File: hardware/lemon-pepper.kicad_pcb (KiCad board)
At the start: 4 copper layers, 35 x 35 mm, 87 parts, among them J101 INPUT, J201 USB_C_Receptacle_USB2.0, J301 TagConnect, J302 USER CONN., M101 MOT, Q501 MMBT5551, SW301 USER, U201 SRV05-4, U301 STM32G431, U302 SN65HVD230, U401 MT6835, U501 MAX15062AATA+T, U601 L6226QTR, U701 MAX49925, U703 MAX49925, Y301 12MHz

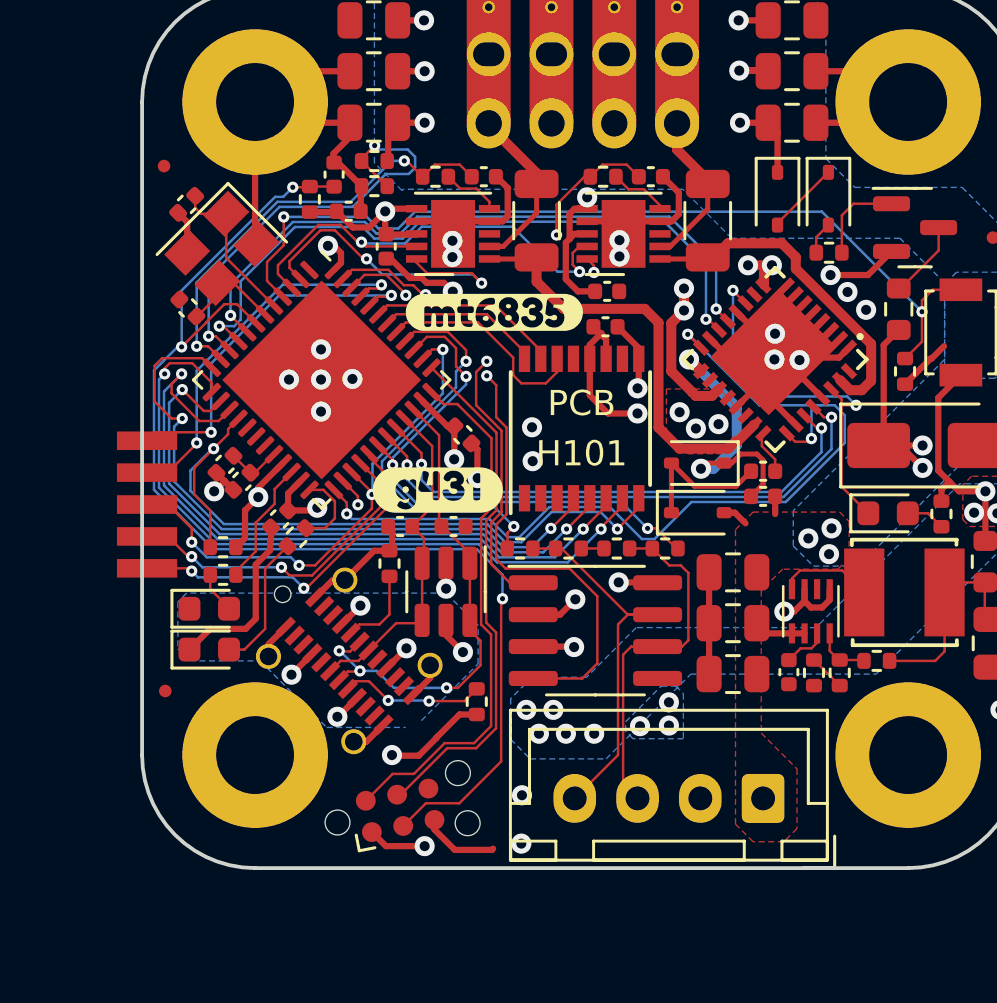
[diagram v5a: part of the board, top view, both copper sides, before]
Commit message: add tooling holes, update CPL
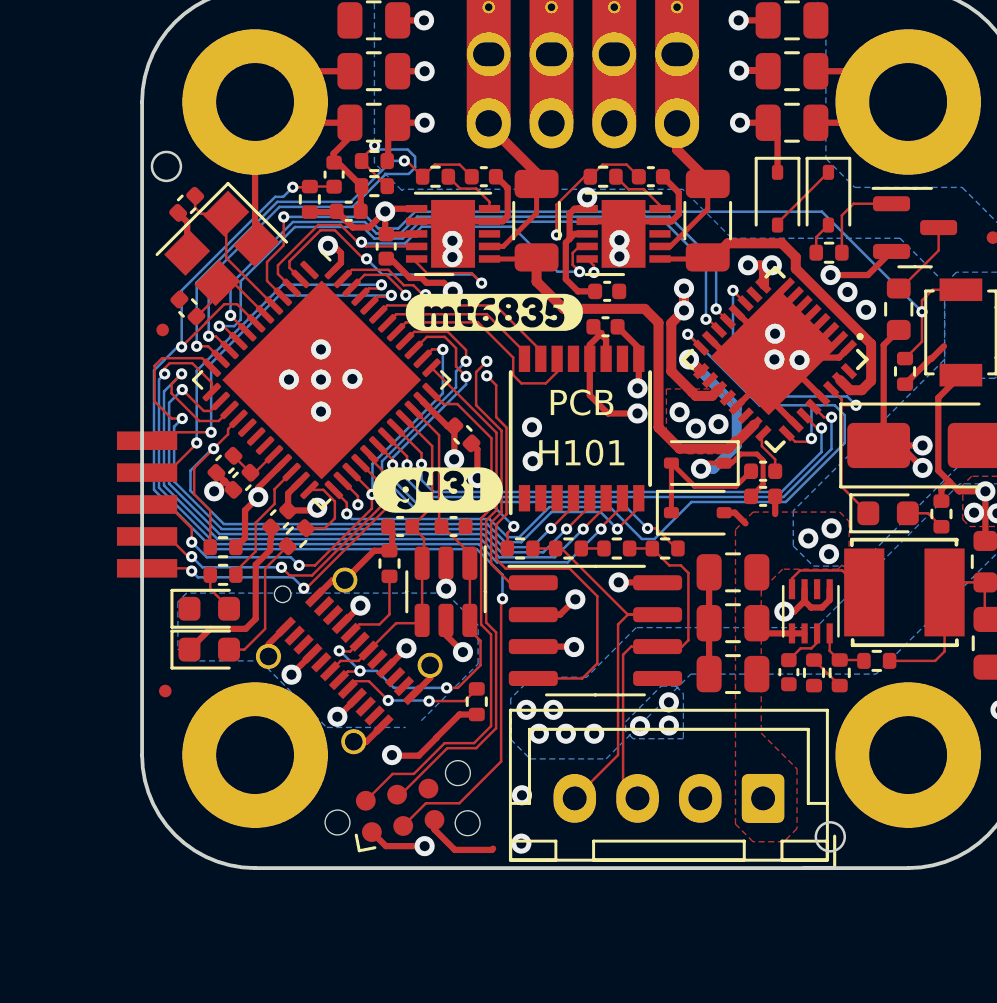
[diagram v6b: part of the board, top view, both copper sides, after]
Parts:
- moved FID101 6.53 mm to (129.6, 83.0)
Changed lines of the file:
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@@
     (property "ki_description" "Generic connector, single row, 01x05, script generated (kicad-library-utils/schlib/autogen/connector/)")
     (property "ki_keywords" "connector")
-    (attr smd exclude_from_bom)
+    (attr smd exclude_from_pos_files exclude_from_bom)
     (fp_text reference "J302" (at 0 -4.235) (layer "F.SilkS") hide
         (effects (font (size 1 1) (thickness 0.15)))
@@
     (property "ki_description" "4-wire bipolar stepper motor")
     (property "ki_keywords" "bipolar stepper motor")
-    (attr through_hole)
+    (attr through_hole exclude_from_pos_files exclude_from_bom)
     (fp_text reference "M101" (at 0 -10 unlocked) (layer "F.SilkS") hide
         (effects (font (size 1 1) (thickness 0.15)))
@@
   )
   (footprint "Fiducial:Fiducial_0.5mm_Mask1mm" (layer "F.Cu")
-    (at 129.675 76.525)
+    (at 129.62 83.05)
     (descr "Circular Fiducial, 0.5mm bare copper, 1mm soldermask opening (Level C)")
     (tags "fiducial")
@@
     (property "ki_description" "Generic connector, single row, 01x04, script generated (kicad-library-utils/schlib/autogen/connector/)")
     (property "ki_keywords" "connector")
-    (attr through_hole)
+    (attr through_hole exclude_from_pos_files exclude_from_bom)
     (fp_text reference "J101" (at 3.75 -3.55 180) (layer "F.SilkS") hide
         (effects (font (size 1 1) (thickness 0.15)))
@@
       (stroke (width 0) (type solid)) (fill solid) (layer "B.SilkS"))
   )
+  (gr_circle (center 129.77 76.54) (end 130.346 76.54)
+    (stroke (width 0.1) (type default)) (fill none) (layer "Edge.Cuts"))
+  (gr_circle (center 156.2 103.23) (end 156.776 103.23)
+    (stroke (width 0.1) (type default)) (fill none) (layer "Edge.Cuts"))
   (gr_text "mj" (at 144.775 87.75) (layer "F.Mask")
     (effects (font (size 1.5 1.5) (thickness 0.3) bold) (justify left bottom))

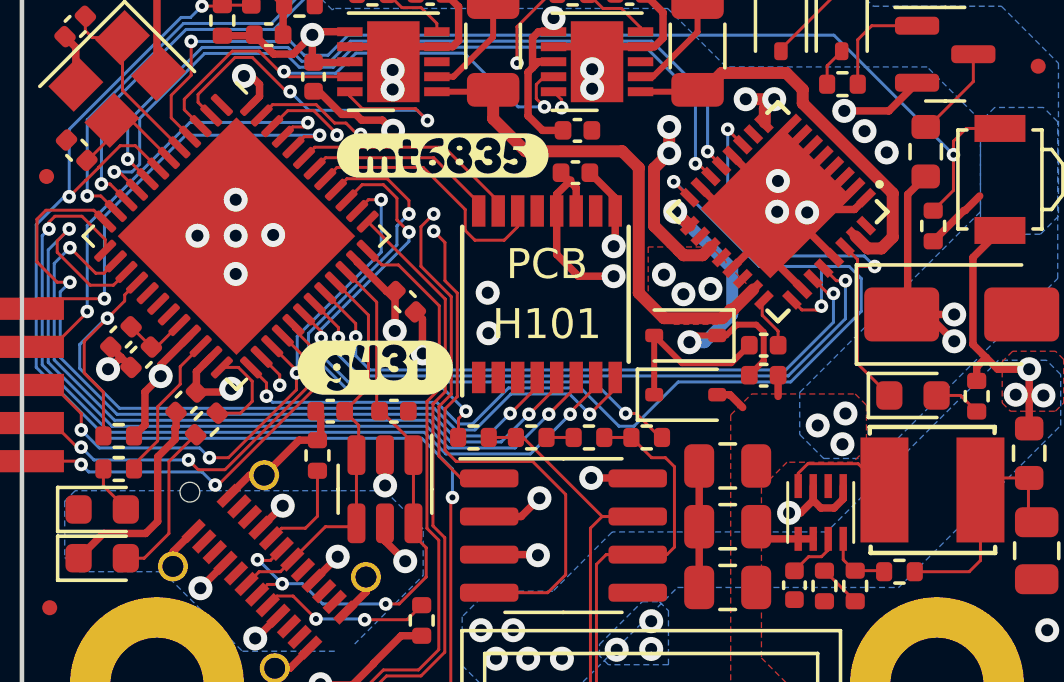
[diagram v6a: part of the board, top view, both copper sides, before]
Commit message: fix erc failures
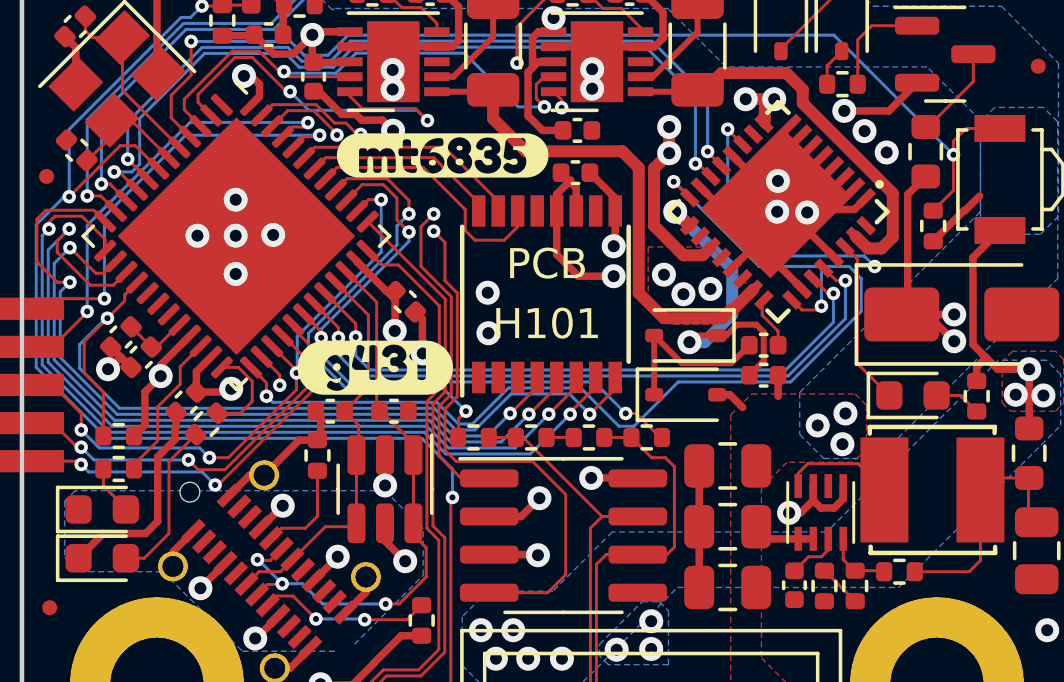
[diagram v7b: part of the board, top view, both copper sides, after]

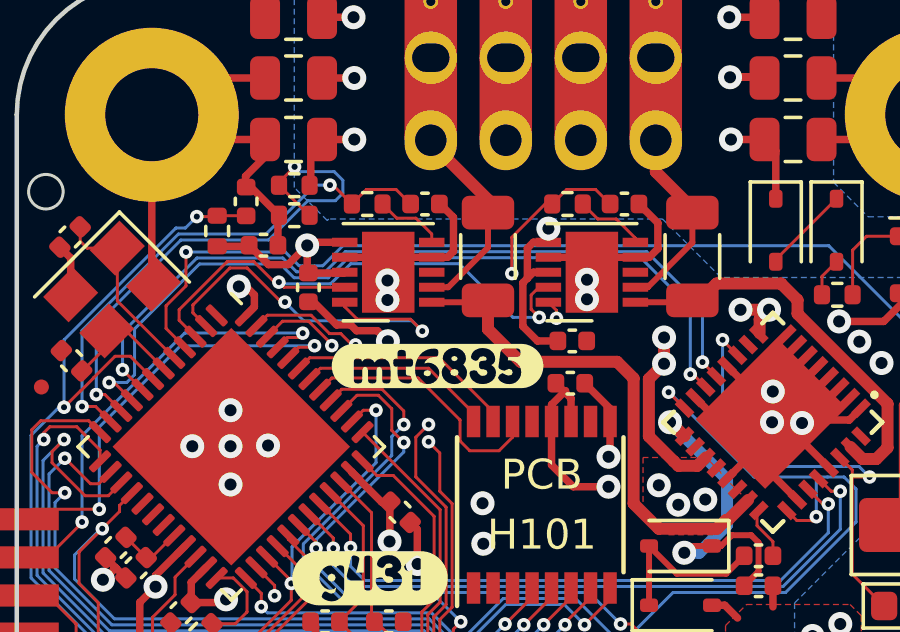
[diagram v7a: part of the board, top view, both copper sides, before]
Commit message: fix current sense pinout
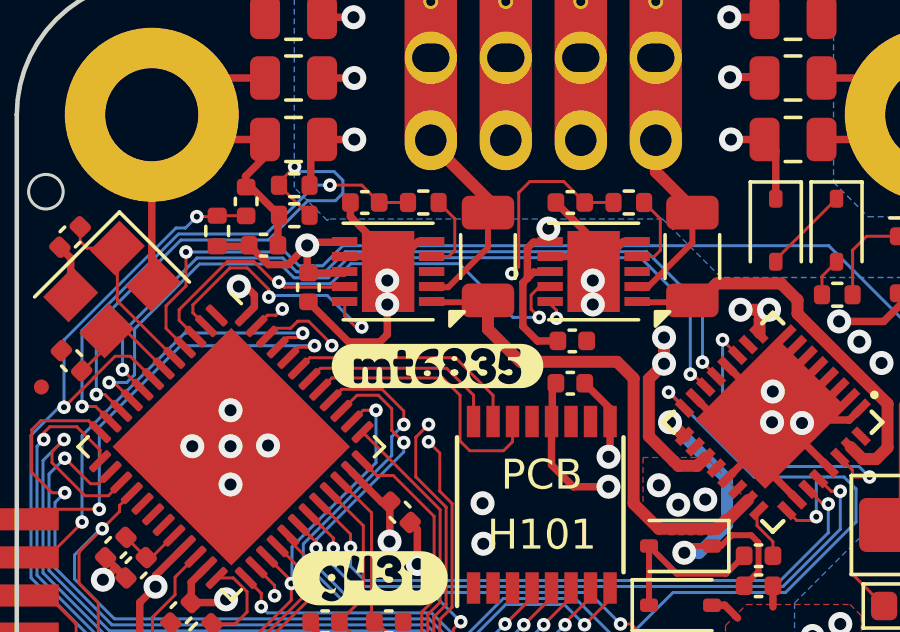
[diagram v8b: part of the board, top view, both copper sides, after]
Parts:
- moved R704 2.04 mm to (149.2, 76.9)
- moved C702 2.01 mm to (140.4, 76.9), turned to 180 degrees
- moved R702 1.87 mm to (142.3, 76.9)
- moved C704 1.81 mm to (147.2, 76.9), turned to 180 degrees
- moved U703 0.06 mm to (148.0, 79.2)
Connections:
- U701 pad 4: GND -> Net-(U701-OUT)
- U701 pad 5: Net-(U701-OUT) -> GND
- U703 pad 4: GND -> Net-(U703-OUT)
- U703 pad 5: Net-(U703-OUT) -> GND
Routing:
- net /current sense/V_SENSE: track 27.0 -> 29.9 mm
- net /encoder/Z: track 8.70 -> 9.27 mm
- net /current sense/U_SENSE: track 17.3 -> 16.8 mm
- net GND: track 132.8 -> 132.9 mm, vias 32 -> 31
- added copper zone on B.Cu, net (none)
- removed copper zone on B.Cu, net Net-(NT701-Pad1)
